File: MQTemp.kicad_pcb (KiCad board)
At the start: 2 copper layers, 48.3 x 45.7 mm, 10 parts, among them J1 Conn_01x02_Male, SW1 SW_DIP_x01

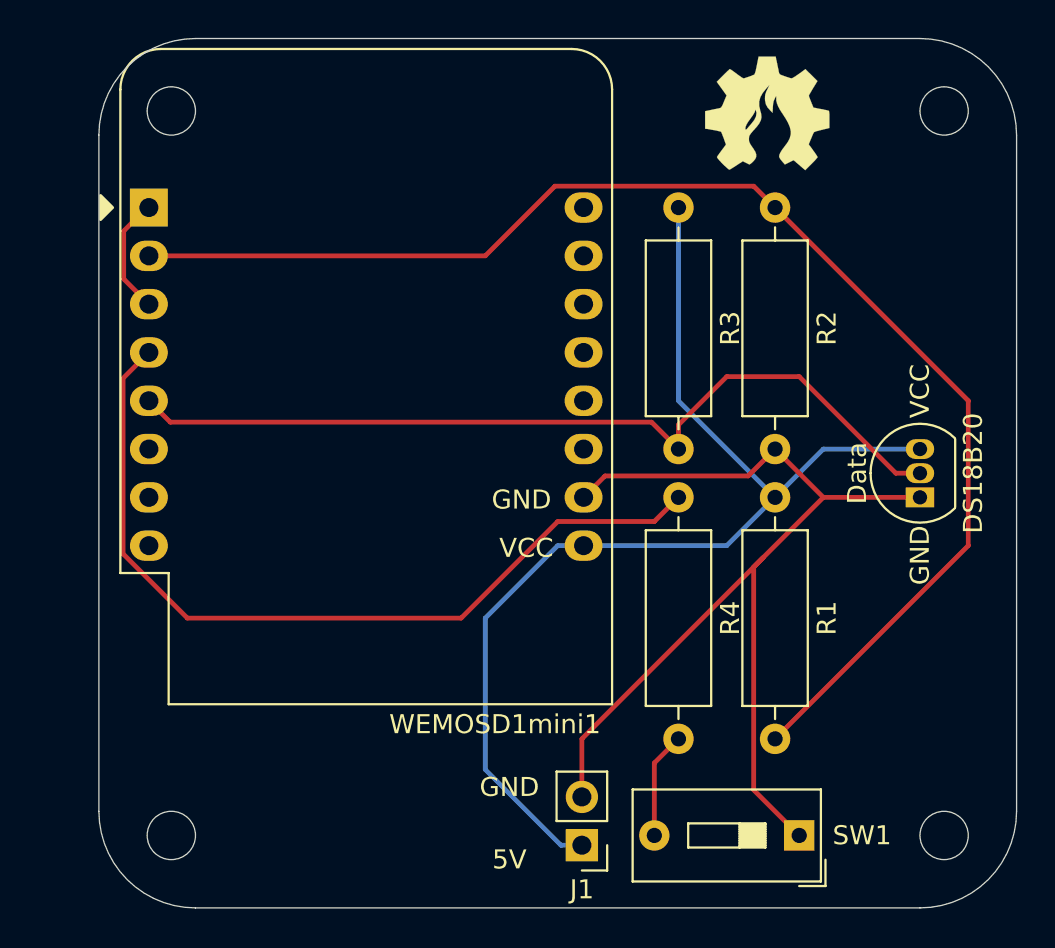
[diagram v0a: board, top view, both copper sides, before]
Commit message: Added space for usb connector
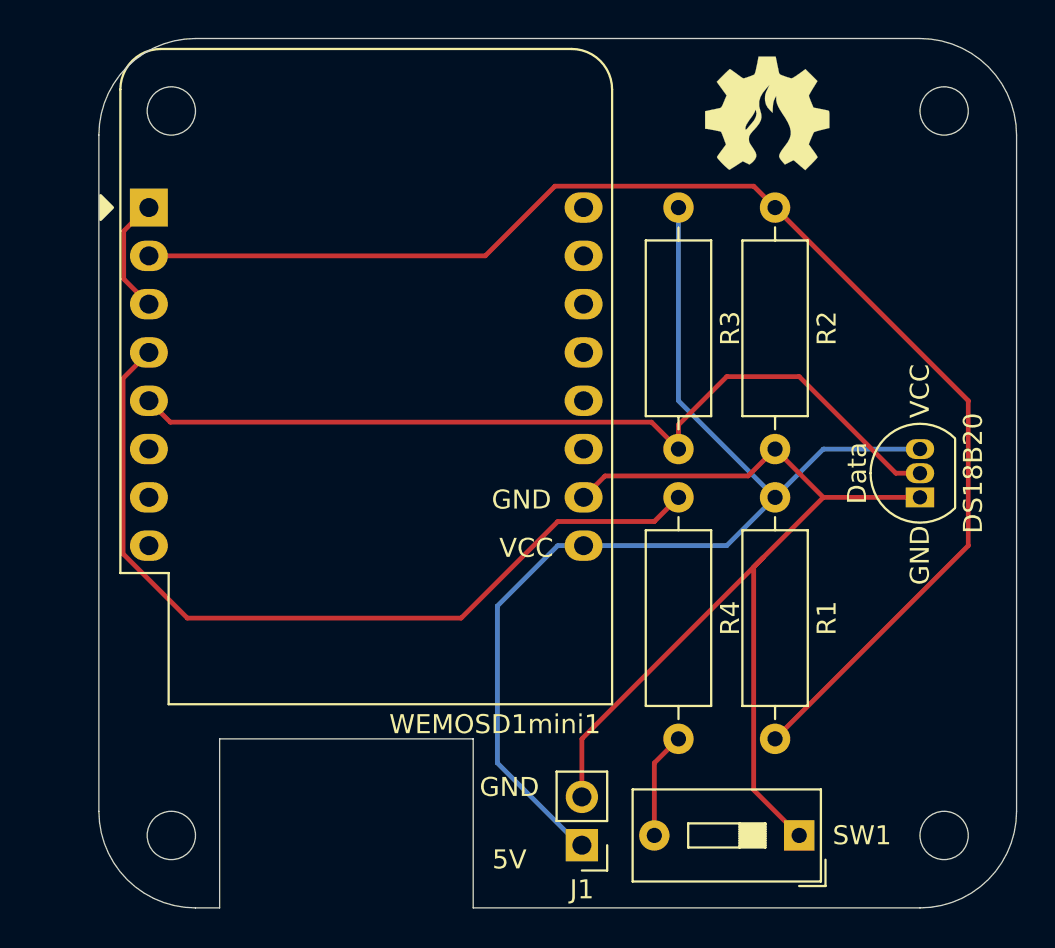
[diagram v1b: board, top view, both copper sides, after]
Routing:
- net VCC: track 58.6 -> 57.5 mm
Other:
- outline, holes or cut-outs redrawn
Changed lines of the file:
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@@
   )
   (gr_rect (start 71.882 39.37) (end 99.06 44.704) (layer "B.SilkS") (width 0.12) (fill none))
-  (gr_line (start 63.5 83.82) (end 101.6 83.82) (layer "Edge.Cuts") (width 0.05))
+  (gr_line (start 101.6 83.82) (end 78.105 83.82) (layer "Edge.Cuts") (width 0.05))
   (gr_arc (start 106.68 78.74) (mid 105.192102 82.332102) (end 101.6 83.82) (layer "Edge.Cuts") (width 0.05))
   (gr_circle (center 102.87 80.01) (end 103.886 79.248) (layer "Edge.Cuts") (width 0.05) (fill none))
@@
   (gr_circle (center 102.87 41.91) (end 104.14 41.91) (layer "Edge.Cuts") (width 0.05) (fill none))
   (gr_line (start 101.6 38.1) (end 63.5 38.1) (layer "Edge.Cuts") (width 0.05))
+  (gr_line (start 63.5 83.82) (end 64.77 83.82) (layer "Edge.Cuts") (width 0.05))
   (gr_line (start 106.68 78.74) (end 106.68 43.18) (layer "Edge.Cuts") (width 0.05))
+  (gr_line (start 64.77 74.93) (end 78.105 74.93) (layer "Edge.Cuts") (width 0.05))
+  (gr_line (start 78.105 74.93) (end 78.105 83.82) (layer "Edge.Cuts") (width 0.05))
+  (gr_line (start 64.77 74.93) (end 64.77 83.82) (layer "Edge.Cuts") (width 0.05))
   (gr_arc (start 63.5 83.82) (mid 59.907898 82.332102) (end 58.42 78.74) (layer "Edge.Cuts") (width 0.05))
   (gr_arc (start 58.42 43.18) (mid 59.907898 39.587898) (end 63.5 38.1) (layer "Edge.Cuts") (width 0.05))
@@
   (segment (start 93.98 74.93) (end 104.14 64.77) (width 0.25) (layer "F.Cu") (net 1))
   (segment (start 82.55 64.77) (end 83.91 64.77) (width 0.25) (layer "B.Cu") (net 2))
-  (segment (start 78.74 76.543) (end 78.74 68.58) (width 0.25) (layer "B.Cu") (net 2))
+  (segment (start 83.698 80.523) (end 79.375 76.2) (width 0.25) (layer "B.Cu") (net 2))
   (segment (start 83.91 64.77) (end 91.44 64.77) (width 0.25) (layer "B.Cu") (net 2))
-  (segment (start 78.74 68.58) (end 82.55 64.77) (width 0.25) (layer "B.Cu") (net 2))
+  (segment (start 79.375 67.945) (end 82.55 64.77) (width 0.25) (layer "B.Cu") (net 2))
+  (segment (start 79.375 76.2) (end 79.375 67.945) (width 0.25) (layer "B.Cu") (net 2))
   (segment (start 93.98 62.23) (end 96.52 59.69) (width 0.25) (layer "B.Cu") (net 2))
   (segment (start 88.9 57.15) (end 88.9 46.99) (width 0.25) (layer "B.Cu") (net 2))
-  (segment (start 82.72 80.523) (end 78.74 76.543) (width 0.25) (layer "B.Cu") (net 2))
   (segment (start 96.52 59.69) (end 101.6 59.69) (width 0.25) (layer "B.Cu") (net 2))
-  (segment (start 83.82 80.523) (end 82.72 80.523) (width 0.25) (layer "B.Cu") (net 2))
   (segment (start 93.98 62.23) (end 88.9 57.15) (width 0.25) (layer "B.Cu") (net 2))
+  (segment (start 83.82 80.523) (end 83.698 80.523) (width 0.25) (layer "B.Cu") (net 2))
   (segment (start 91.44 64.77) (end 93.98 62.23) (width 0.25) (layer "B.Cu") (net 2))
   (segment (start 83.82 77.983) (end 83.82 74.93) (width 0.25) (layer "F.Cu") (net 3))

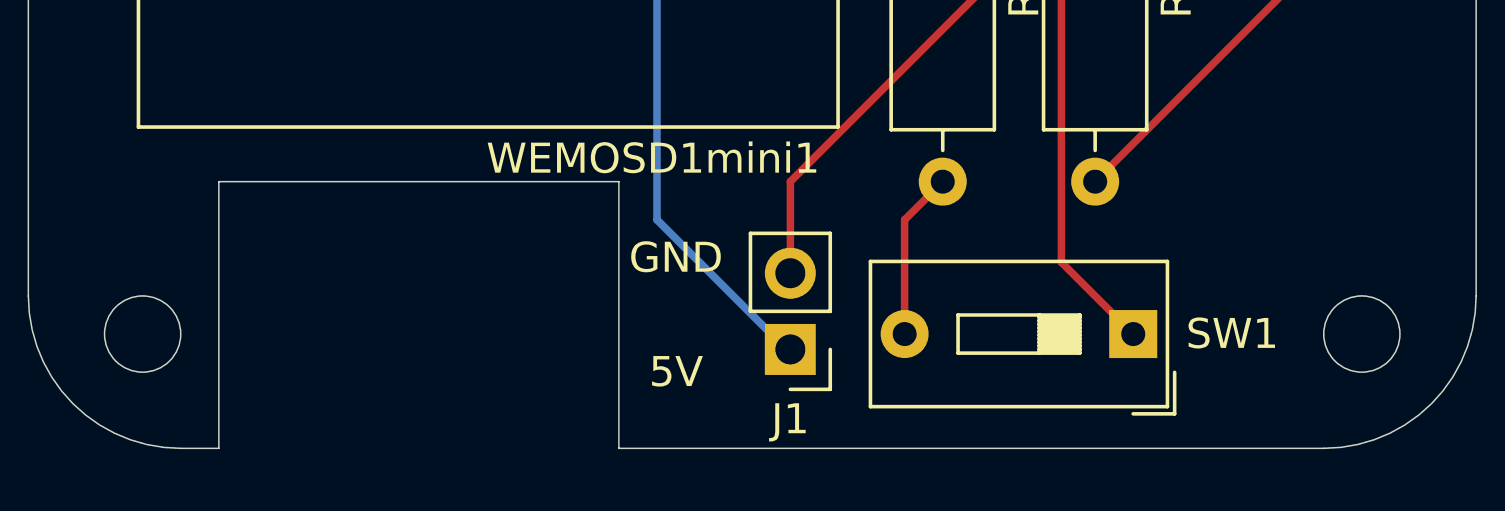
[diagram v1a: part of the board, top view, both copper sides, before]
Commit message: Connector placed and spacer rounded
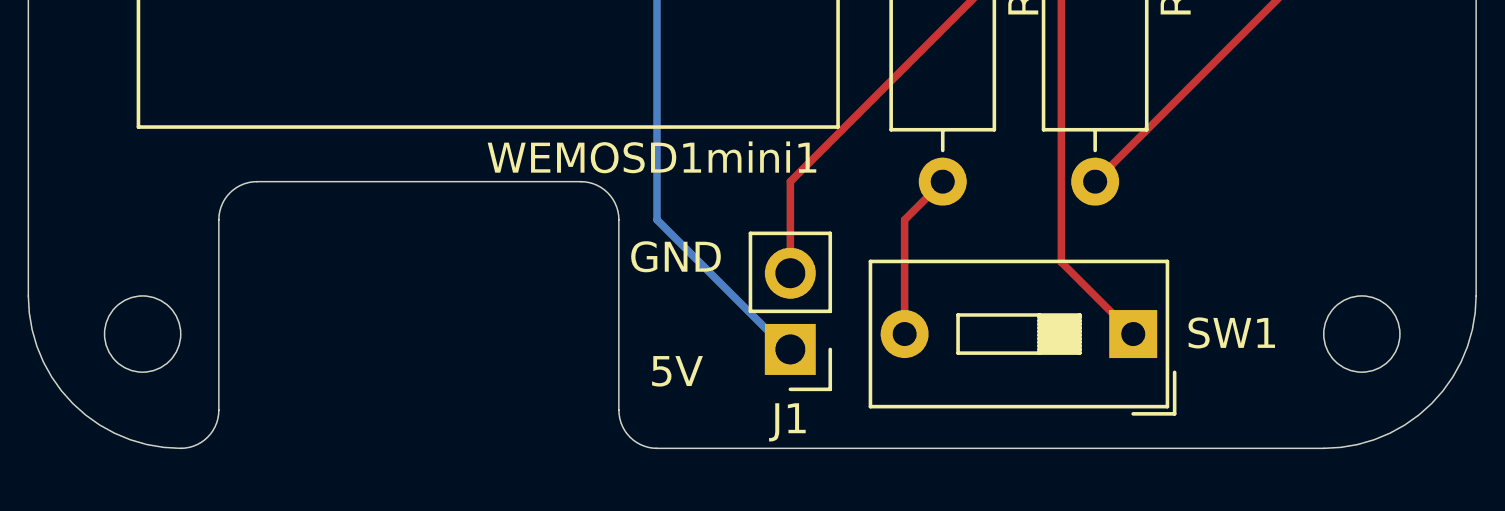
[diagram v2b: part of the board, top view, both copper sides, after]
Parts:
- moved G*** 0.97 mm to (70.8, 56.5)
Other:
- outline, holes or cut-outs redrawn
- board text added: "A0"
- board text added: "D5"
- board text added: "D6"
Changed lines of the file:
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@@
   )
   (footprint "logos:mark-20mm" (layer "B.Cu")
-    (at 69.878144 56.134 180)
+    (at 70.767144 56.515 180)
     (attr through_hole)
     (fp_text reference "G***" (at 0 0) (layer "B.SilkS") hide
@@
   )
   (gr_rect (start 71.882 39.37) (end 99.06 44.704) (layer "B.SilkS") (width 0.12) (fill none))
-  (gr_line (start 101.6 83.82) (end 78.105 83.82) (layer "Edge.Cuts") (width 0.05))
+  (gr_line (start 101.6 83.82) (end 79.375 83.82) (layer "Edge.Cuts") (width 0.05))
   (gr_arc (start 106.68 78.74) (mid 105.192102 82.332102) (end 101.6 83.82) (layer "Edge.Cuts") (width 0.05))
   (gr_circle (center 102.87 80.01) (end 103.886 79.248) (layer "Edge.Cuts") (width 0.05) (fill none))
   (gr_arc (start 101.6 38.1) (mid 105.192102 39.587898) (end 106.68 43.18) (layer "Edge.Cuts") (width 0.05))
+  (gr_arc (start 79.375 83.82) (mid 78.476974 83.448026) (end 78.105 82.55) (layer "Edge.Cuts") (width 0.05))
+  (gr_arc (start 64.77 76.2) (mid 65.141974 75.301974) (end 66.04 74.93) (layer "Edge.Cuts") (width 0.05))
   (gr_circle (center 62.23 41.91) (end 63.5 41.91) (layer "Edge.Cuts") (width 0.05) (fill none))
   (gr_circle (center 102.87 41.91) (end 104.14 41.91) (layer "Edge.Cuts") (width 0.05) (fill none))
   (gr_line (start 101.6 38.1) (end 63.5 38.1) (layer "Edge.Cuts") (width 0.05))
-  (gr_line (start 63.5 83.82) (end 64.77 83.82) (layer "Edge.Cuts") (width 0.05))
+  (gr_arc (start 76.835 74.93) (mid 77.733026 75.301974) (end 78.105 76.2) (layer "Edge.Cuts") (width 0.05))
+  (gr_arc (start 64.77 82.55) (mid 64.398026 83.448026) (end 63.5 83.82) (layer "Edge.Cuts") (width 0.05))
   (gr_line (start 106.68 78.74) (end 106.68 43.18) (layer "Edge.Cuts") (width 0.05))
-  (gr_line (start 64.77 74.93) (end 78.105 74.93) (layer "Edge.Cuts") (width 0.05))
-  (gr_line (start 78.105 74.93) (end 78.105 83.82) (layer "Edge.Cuts") (width 0.05))
-  (gr_line (start 64.77 74.93) (end 64.77 83.82) (layer "Edge.Cuts") (width 0.05))
+  (gr_line (start 66.04 74.93) (end 76.835 74.93) (layer "Edge.Cuts") (width 0.05))
+  (gr_line (start 78.105 76.2) (end 78.105 82.55) (layer "Edge.Cuts") (width 0.05))
+  (gr_line (start 64.77 76.2) (end 64.77 82.55) (layer "Edge.Cuts") (width 0.05))
   (gr_arc (start 63.5 83.82) (mid 59.907898 82.332102) (end 58.42 78.74) (layer "Edge.Cuts") (width 0.05))
   (gr_arc (start 58.42 43.18) (mid 59.907898 39.587898) (end 63.5 38.1) (layer "Edge.Cuts") (width 0.05))
   (gr_line (start 58.42 43.18) (end 58.42 78.74) (layer "Edge.Cuts") (width 0.05))
   (gr_circle (center 62.23 80.01) (end 63.5 80.01) (layer "Edge.Cuts") (width 0.05) (fill none))
+  (gr_text "A0" (at 63.5 49.53) (layer "B.SilkS")
+    (effects (font (size 1 1) (thickness 0.15)) (justify mirror))
+  )
+  (gr_text "GND" (at 86.995 62.23) (layer "B.SilkS")
+    (effects (font (size 1 1) (thickness 0.15)) (justify mirror))
+  )
+  (gr_text "D6" (at 63.5 57.15) (layer "B.SilkS")
+    (effects (font (size 1 1) (thickness 0.15)) (justify mirror))
+  )
   (gr_text "${TITLE}\n${REVISION}\n${ISSUE_DATE}" (at 98.552 41.91) (layer "B.SilkS")
     (effects (font (size 1 1) (thickness 0.15)) (justify left mirror))
   )
+  (gr_text "VCC" (at 86.995 64.77) (layer "B.SilkS")
+    (effects (font (size 1 1) (thickness 0.15)) (justify mirror))
+  )
+  (gr_text "D5" (at 63.5 54.61) (layer "B.SilkS")
+    (effects (font (size 1 1) (thickness 0.15)) (justify mirror))
+  )
   (gr_text "GND" (at 101.6 65.278 90) (layer "F.SilkS")

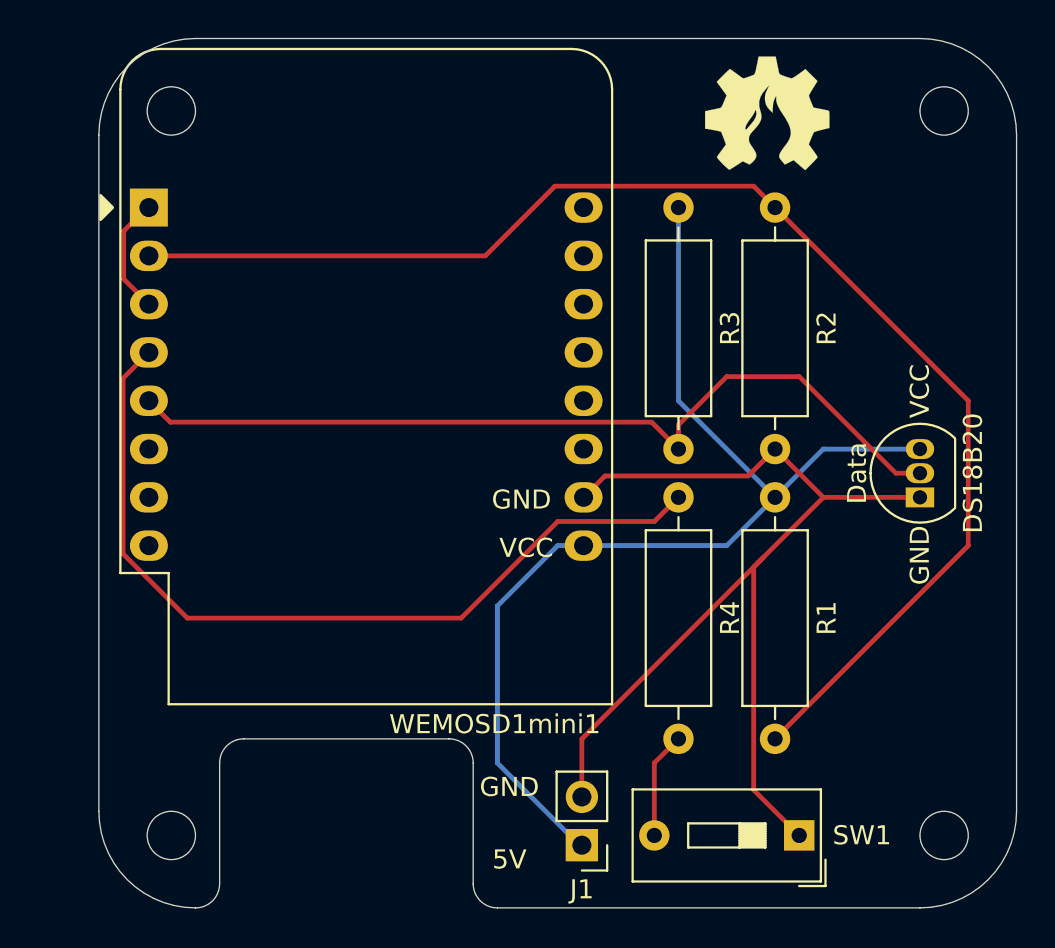
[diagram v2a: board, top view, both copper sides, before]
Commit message: Smaller footprints. More compact design
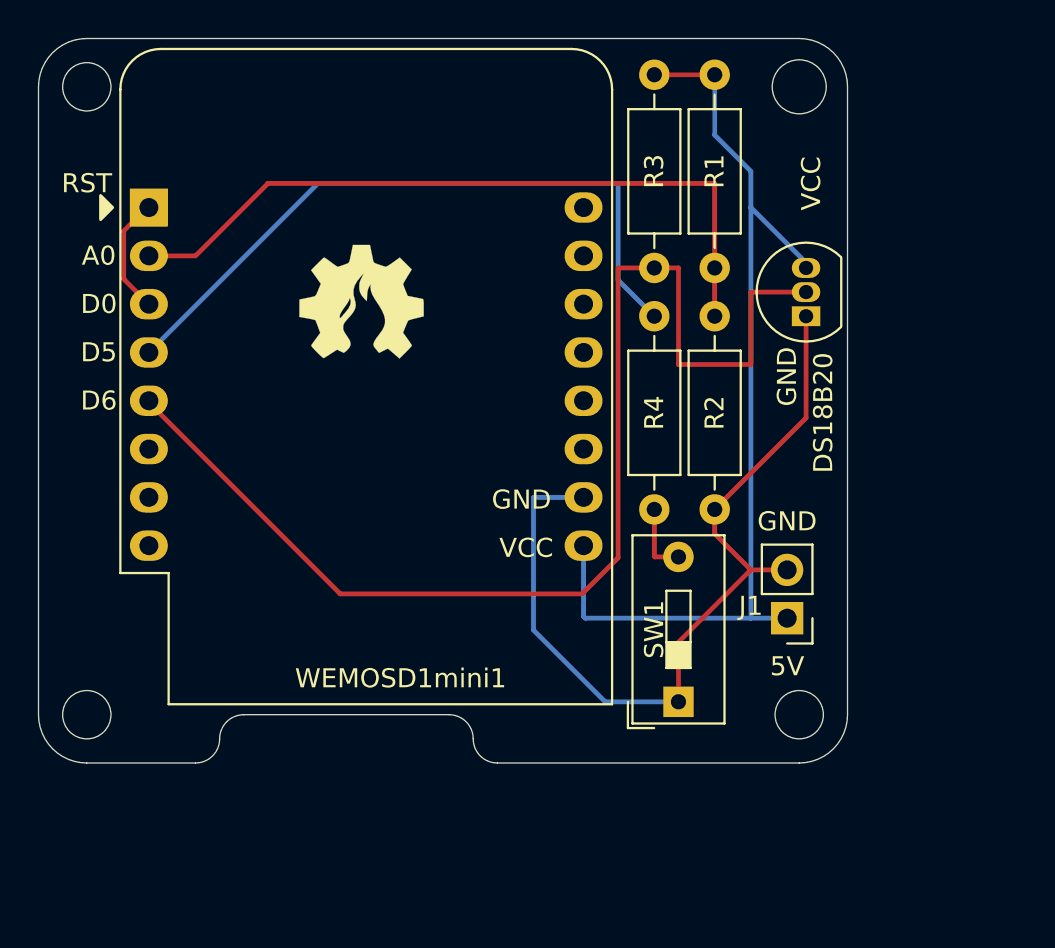
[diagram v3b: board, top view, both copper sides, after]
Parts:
- R1, R2, R3, R4: footprint Resistor_THT:R_Axial_DIN0309_L9.0mm_D3.2mm_P12.70mm_Horizontal -> Resistor_THT:R_Axial_DIN0207_L6.3mm_D2.5mm_P10.16mm_Horizontal
- moved GOHL 23.5 mm to (72.4, 52.1)
- moved R1 22.5 mm to (90.8, 40.0)
- moved J1 16.1 mm to (94.6, 68.6)
- moved DS18B20 11.3 mm to (95.6, 52.7)
- moved R4 9.61 mm to (87.6, 52.7)
- moved SW1 9.47 mm to (88.9, 73.0), turned to 90 degrees
- moved R3 7.10 mm to (87.6, 40.0)
- moved R2 6.54 mm to (90.8, 52.7)
- moved GFACE 0.64 mm to (70.1, 56.5)
- renumbered G*** to GFACE, G*** to GOHL
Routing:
- net Net-(R1-Pad2): track 71.3 -> 38.3 mm
- net /D6: track 46.0 -> 63.7 mm
- net GND: track 56.6 -> 45.3 mm
- net /D5: track 44.4 -> 36.1 mm
- net VCC: track 57.5 -> 51.4 mm
- net Net-(R4-Pad2): track 5.61 -> 3.74 mm
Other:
- board size 48.3 x 45.7 mm -> 42.5 x 38.1 mm
- board text added: "D0"
- board text added: "RST"
- board text removed: "Data"
